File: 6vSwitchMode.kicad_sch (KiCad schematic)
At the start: 27 parts, among them IC2 TPS40192DRCT-TPS40192DRCT, Q3 BUK9M17-30EX / BUK7M10-40E, Q4 BUK9M17-30EX / BUK7M10-40E

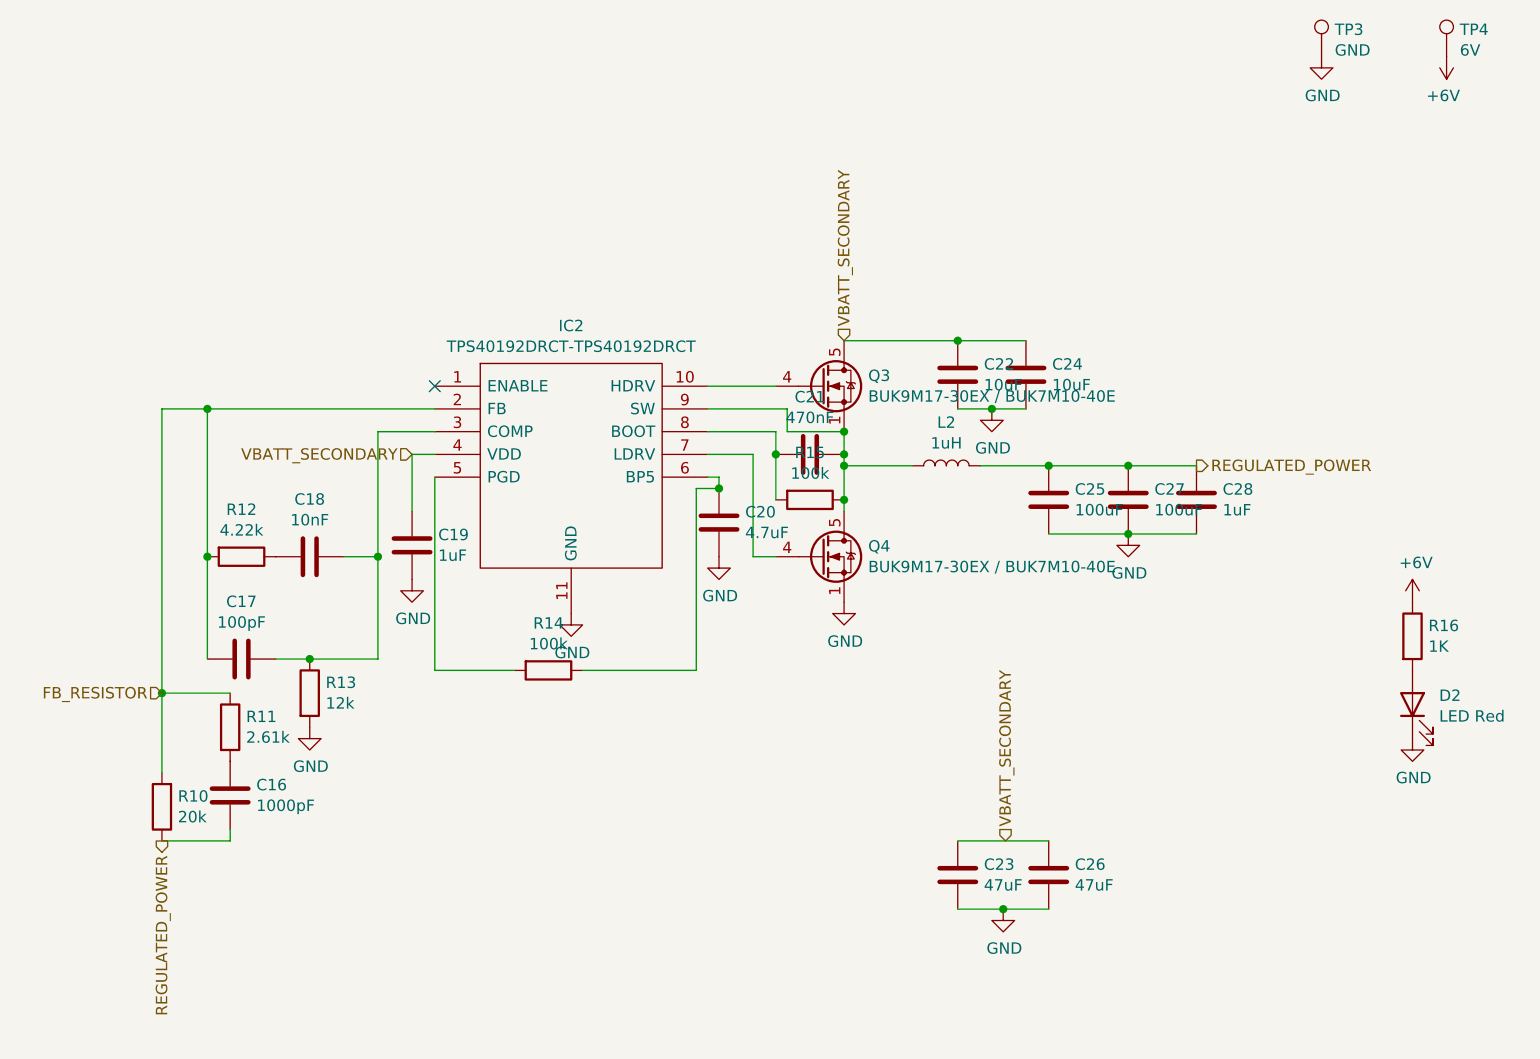
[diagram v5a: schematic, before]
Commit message: routing finished, had to use in 1 for some signals :(
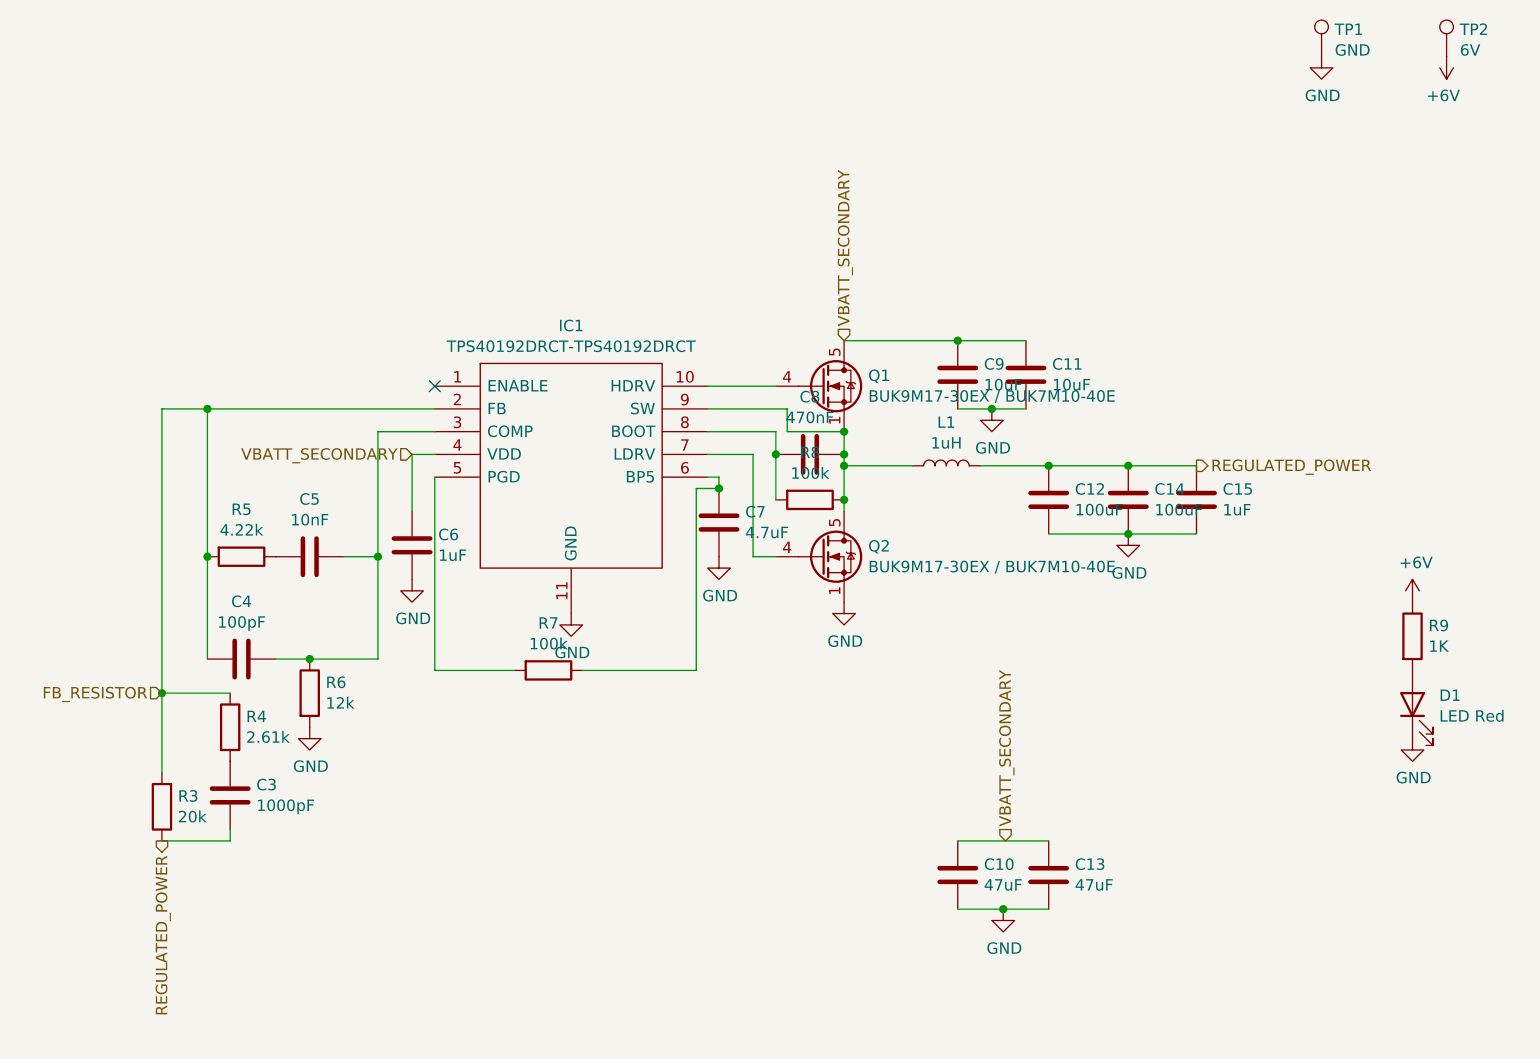
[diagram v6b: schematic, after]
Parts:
- renumbered C23 to C10, C24 to C11, C25 to C12, C26 to C13, C27 to C14, C28 to C15, C16 to C3, C17 to C4, C18 to C5, C19 to C6, C20 to C7, C21 to C8, C22 to C9, D2 to D1, IC2 to IC1, L2 to L1, Q3 to Q1, Q4 to Q2, R10 to R3, R11 to R4, R12 to R5, R13 to R6, R14 to R7, R15 to R8, R16 to R9, TP3 to TP1, TP4 to TP2
